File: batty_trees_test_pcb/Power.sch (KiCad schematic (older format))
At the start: 44 parts

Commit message: Finished off Power section and made up AFE schematic
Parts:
- removed J? (x3): Jumper, Connector_PinHeader_2.54mm:PinHeader_1x02_P2.54mm_Vertical, symbol Connector:Conn_01x02_Male
- added C?: 4.7uF, Capacitor_SMD:C_0805_2012Metric_Pad1.15x1.40mm_HandSolder, symbol Device:C_Small
- added C?: 0.1uF, Capacitor_SMD:C_0805_2012Metric_Pad1.15x1.40mm_HandSolder, symbol Device:C_Small
- added JP? (x4): Jumper, Connector_PinHeader_2.54mm:PinHeader_1x02_P2.54mm_Vertical, symbol Device:Jumper_NO_Small
- added R? (x3): 10k, Capacitor_SMD:C_0805_2012Metric_Pad1.15x1.40mm_HandSolder, symbol Device:R
- added TP? (x4): Test Point, OSU_SIM_BASIC:Keystone_5019, symbol Connector:TestPoint_Alt
- added U?: AD8031, Package_TO_SOT_SMD:SOT-23-5, symbol OSU_SIM_FULL:AD8031
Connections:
- net labels added: VMID
- wire segments 163 -> 185
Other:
- note added: "Alt micro USB for power"
- note added: "Buffer to supply 1/2 VDDA for VGR and AFE"
- moved on the sheet: R?, TP?

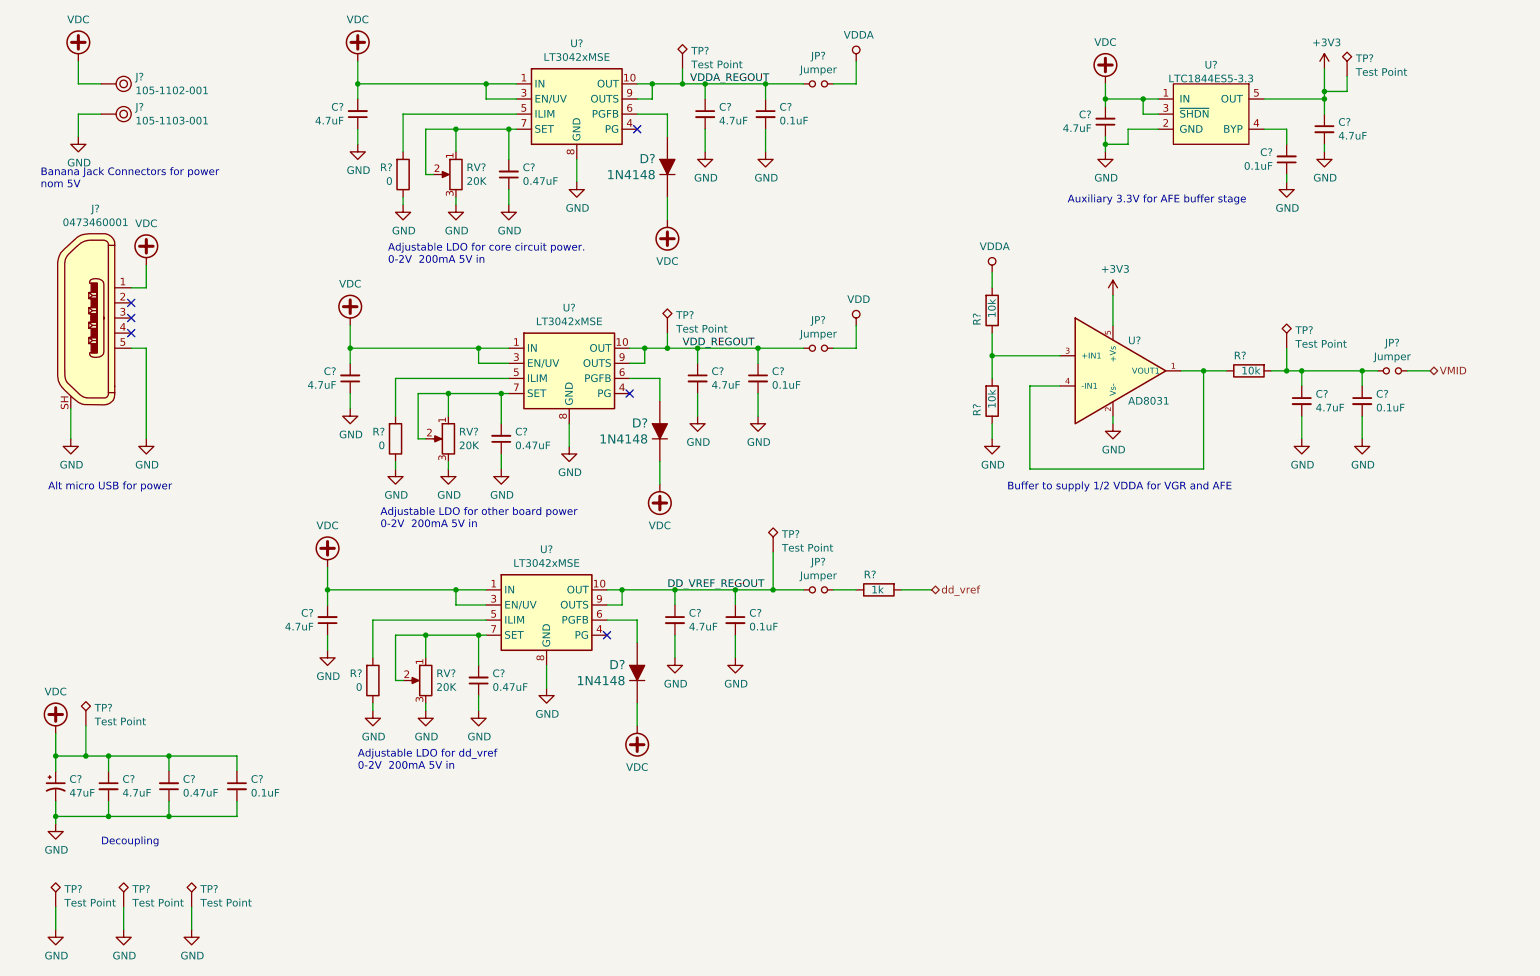
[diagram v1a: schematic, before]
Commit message: wired up chip to fpga on schematic and begininng to do layout
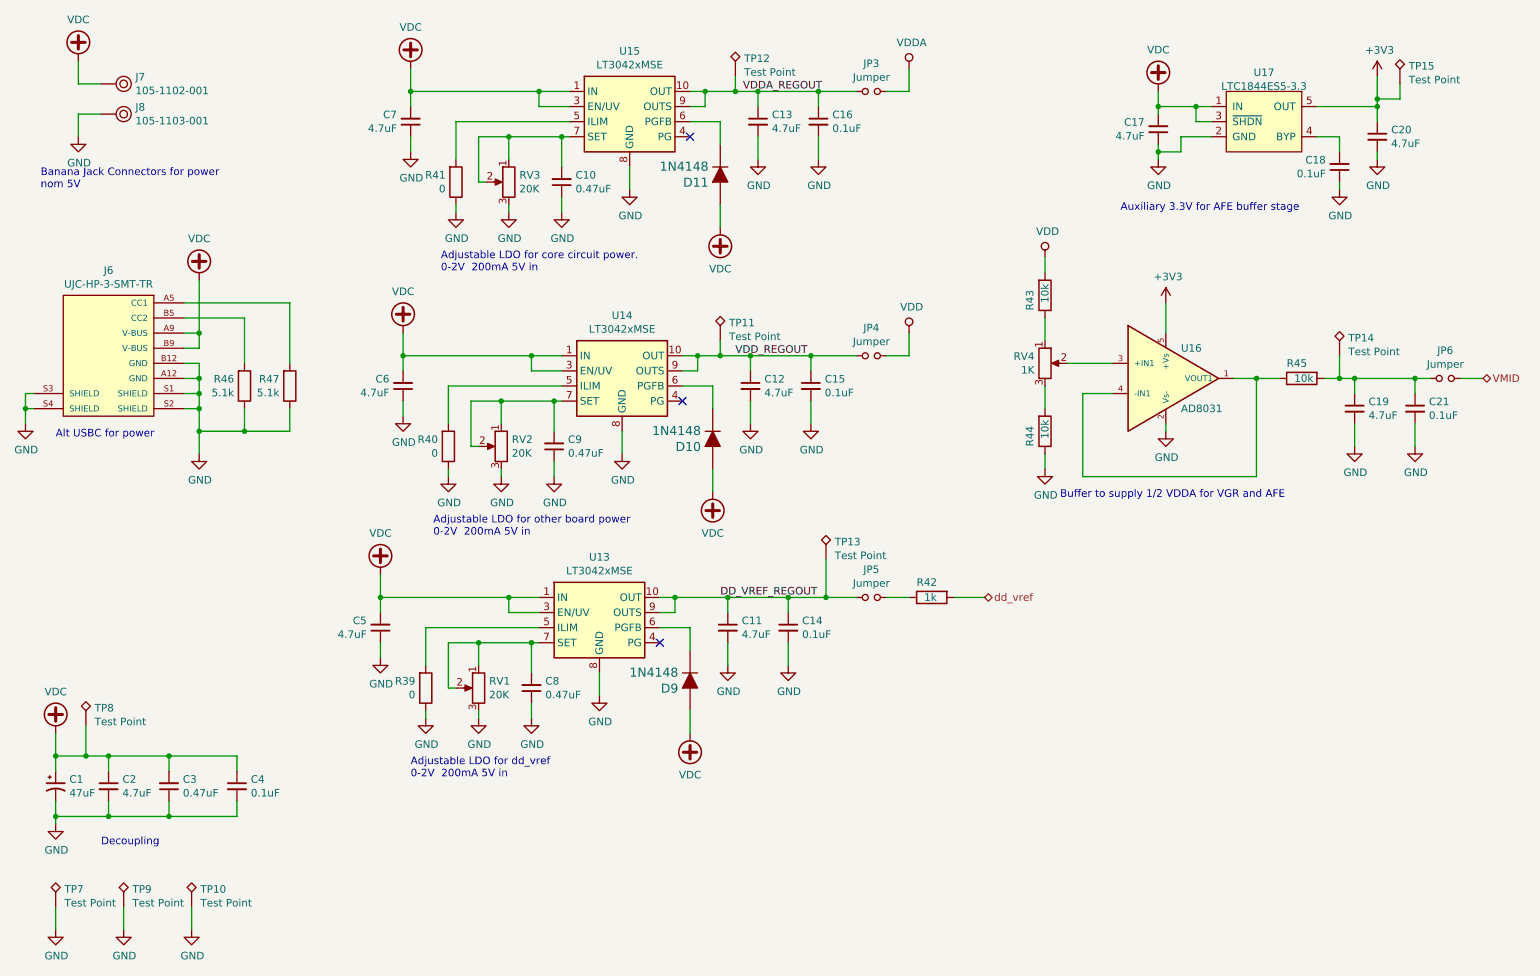
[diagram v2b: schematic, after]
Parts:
- removed J?: 0473460001, digikey-footprints:USB_Micro_B_Female_0473460001, symbol dk_USB-DVI-HDMI-Connectors:0473460001
- added J6: UJC-HP-3-SMT-TR, CUI_UJC-HP-3-SMT-TR, symbol OSU_SIM_FULL:UJC-HP-3-SMT-TR
- added R46, R47: 5.1k, Capacitor_SMD:C_0805_2012Metric_Pad1.15x1.40mm_HandSolder, symbol Device:R
- added RV4: 1K, Potentiometer_THT:Potentiometer_Bourns_3266W_Vertical, symbol Device:R_POT
- gave numbers to parts that had none: 54
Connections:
- net GND: now also J6.A12 (GND), J6.B12 (GND), J6.S1 (SHIELD), J6.S2 (SHIELD), J6.S3 (SHIELD), J6.S4 (SHIELD), R46.1, R47.1
- net VDC: now also D10.A, D11.A, D9.A, J6.A9 (V-BUS), J6.B9 (V-BUS); no longer D10.K, D11.K, D9.K
- net VDD: now also R43.2
- net VDDA: no longer R43.2
- net at U13.6 (PGFB): now also D9.K; no longer D9.A
- net at U15.6 (PGFB): now also D11.K; no longer D11.A
- net at U14.6 (PGFB): now also D10.K; no longer D10.A
- new net: J6.A5 (CC1), R47.2
- new net: J6.B5 (CC2), R46.2
- new net: RV4.2, U16.3 (+IN1)
- new net: R43.1, RV4.1
- new net: R44.2, RV4.3
- no-connect marks 6 -> 3
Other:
- note added: "Alt USBC for power"
- note removed: "Alt micro USB for power"
- moved on the sheet: C10, C11, C12, C13, C14, C15, C16, C17, C18, C19, C20, C21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

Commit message: more layout work ~90% finished
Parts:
- added C22: 0.1uF, Capacitor_SMD:C_0805_2012Metric_Pad1.15x1.40mm_HandSolder, symbol Device:C_Small
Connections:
- net +3V3: now also C22.1
- net DD_VREF_REGOUT: now also R42.1; no longer JP5.1
- net GND: now also C22.2
- net dd_vref: now also JP5.2; no longer R42.2
- new net: JP5.1, R42.2
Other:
- moved on the sheet: JP5, R42
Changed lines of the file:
@@
 	5600 4550 5850 4550
 Connection ~ 5600 4550
-Wire Wire Line
-	6250 4550 6400 4550
 $Comp
 L Device:R R42
 U 1 1 5F3F702F
-P 6550 4550
-F 0 "R42" V 6450 4650 50  0000 R CNN
-F 1 "1k" V 6550 4600 50  0000 R CNN
-F 2 "Capacitor_SMD:C_0805_2012Metric_Pad1.15x1.40mm_HandSolder" V 6480 4550 50  0001 C CNN
-F 3 "~" H 6550 4550 50  0001 C CNN
-	1    6550 4550
+P 6100 4550
+F 0 "R42" V 6000 4650 50  0000 R CNN
+F 1 "1k" V 6100 4600 50  0000 R CNN
+F 2 "Capacitor_SMD:C_0805_2012Metric_Pad1.15x1.40mm_HandSolder" V 6030 4550 50  0001 C CNN
+F 3 "~" H 6100 4550 50  0001 C CNN
+	1    6100 4550
 	0    -1   1    0
 $EndComp
@@
 L Device:Jumper_NO_Small JP5
 U 1 1 5F454C9C
-P 6150 4550
-F 0 "JP5" H 6150 4735 50  0000 C CNN
-F 1 "Jumper" H 6150 4644 50  0000 C CNN
-F 2 "Connector_PinHeader_2.54mm:PinHeader_1x02_P2.54mm_Vertical" H 6150 4550 50  0001 C CNN
-F 3 "~" H 6150 4550 50  0001 C CNN
-	1    6150 4550
+P 6500 4550
+F 0 "JP5" H 6500 4735 50  0000 C CNN
+F 1 "Jumper" H 6500 4644 50  0000 C CNN
+F 2 "Connector_PinHeader_2.54mm:PinHeader_1x02_P2.54mm_Vertical" H 6500 4550 50  0001 C CNN
+F 3 "~" H 6500 4550 50  0001 C CNN
+	1    6500 4550
 	1    0    0    -1
 $EndComp
@@
 Wire Wire Line
 	5250 1200 5400 1200
-Connection ~ 5850 4550
-Wire Wire Line
-	5850 4550 6050 4550
-Wire Wire Line
-	6700 4550 6900 4550
+Wire Wire Line
+	6600 4550 6900 4550
 $Comp
 L Connector:TestPoint_Alt TP14
@@
 Wire Wire Line
 	7450 3000 7750 3000
+Wire Wire Line
+	5850 4550 5950 4550
+Connection ~ 5850 4550
+Wire Wire Line
+	6250 4550 6400 4550
+$Comp
+L Device:C_Small C22
+U 1 1 5F53F49B
+P 8550 2600
+F 0 "C22" H 8458 2646 50  0000 R CNN
+F 1 "0.1uF" H 8458 2555 50  0000 R CNN
+F 2 "Capacitor_SMD:C_0805_2012Metric_Pad1.15x1.40mm_HandSolder" H 8550 2600 50  0001 C CNN
+F 3 "~" H 8550 2600 50  0001 C CNN
+F 4 "399-8000-1-ND" H 8550 2600 50  0001 C CNN "Digi-Key_PN"
+	1    8550 2600
+	-1   0    0    -1
+$EndComp
+$Comp
+L power:+3V3 #PWR0144
+U 1 1 5F541480
+P 8550 2450
+F 0 "#PWR0144" H 8550 2300 50  0001 C CNN
+F 1 "+3V3" H 8565 2623 50  0000 C CNN
+F 2 "" H 8550 2450 50  0001 C CNN
+F 3 "" H 8550 2450 50  0001 C CNN
+	1    8550 2450
+	1    0    0    -1
+$EndComp
+$Comp
+L power:GND #PWR0145
+U 1 1 5F54D21D
+P 8550 2800
+F 0 "#PWR0145" H 8550 2550 50  0001 C CNN
+F 1 "GND" H 8555 2627 50  0000 C CNN
+F 2 "" H 8550 2800 50  0001 C CNN
+F 3 "" H 8550 2800 50  0001 C CNN
+	1    8550 2800
+	1    0    0    -1
+$EndComp
+Wire Wire Line
+	8550 2500 8550 2450
+Wire Wire Line
+	8550 2800 8550 2700
 $EndSCHEMATC

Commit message: Layout finished and gerbers generated checking for DFM
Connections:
- net GND: no longer J6.S1 (SHIELD), J6.S2 (SHIELD), J6.S3 (SHIELD), J6.S4 (SHIELD)
- no-connect marks 3 -> 7
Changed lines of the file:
@@
 Banana Jack Connectors for power\nnom 5V\n
-$Comp
-L power:GND #PWR075
-U 1 1 5F54C291
-P 550 3400
-F 0 "#PWR075" H 550 3150 50  0001 C CNN
-F 1 "GND" H 555 3227 50  0000 C CNN
-F 2 "" H 550 3400 50  0001 C CNN
-F 3 "" H 550 3400 50  0001 C CNN
-	1    550  3400
-	1    0    0    -1
-$EndComp
-Wire Wire Line
-	550  3200 550  3300
 $Comp
 L power:GND #PWR080
@@
 	1600 3100 1700 3100
 Connection ~ 1700 3100
-Wire Wire Line
-	1700 3100 1700 3200
-Wire Wire Line
-	1600 3200 1700 3200
-Connection ~ 1700 3200
-Wire Wire Line
-	1700 3200 1700 3300
-Connection ~ 1700 3300
-Wire Wire Line
-	1700 3300 1700 3450
-Wire Wire Line
-	1600 3300 1700 3300
-Wire Wire Line
-	600  3200 550  3200
-Wire Wire Line
-	600  3300 550  3300
-Connection ~ 550  3300
-Wire Wire Line
-	550  3300 550  3400
 $Comp
 L Device:R R46
@@
 Wire Wire Line
 	8550 2800 8550 2700
+NoConn ~ 600  3300
+NoConn ~ 600  3200
+Wire Wire Line
+	1700 3100 1700 3450
+NoConn ~ 1600 3200
+NoConn ~ 1600 3300
 $EndSCHEMATC

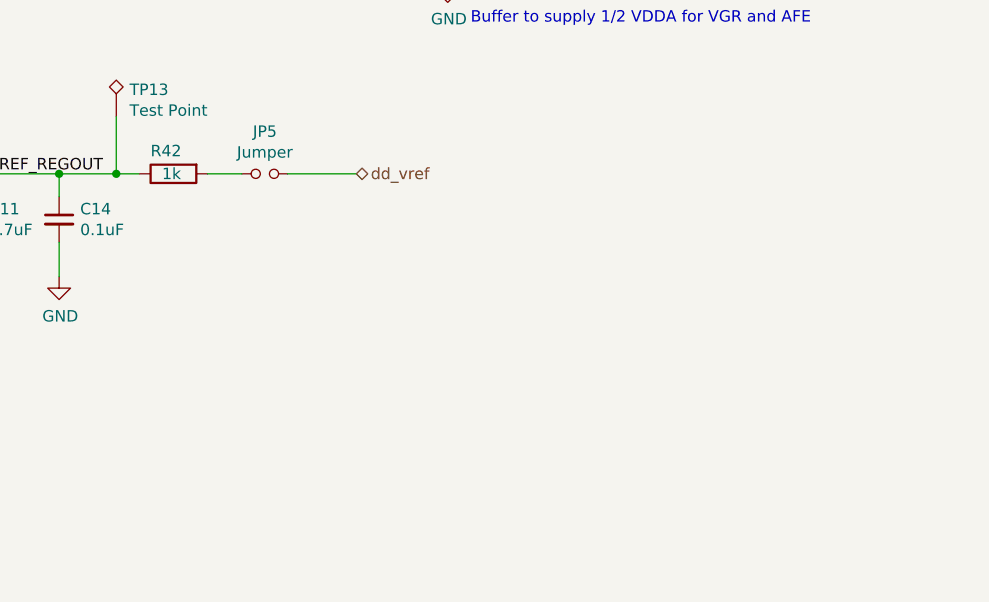
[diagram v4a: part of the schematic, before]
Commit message: all componenets updated with digikey pn bom generated
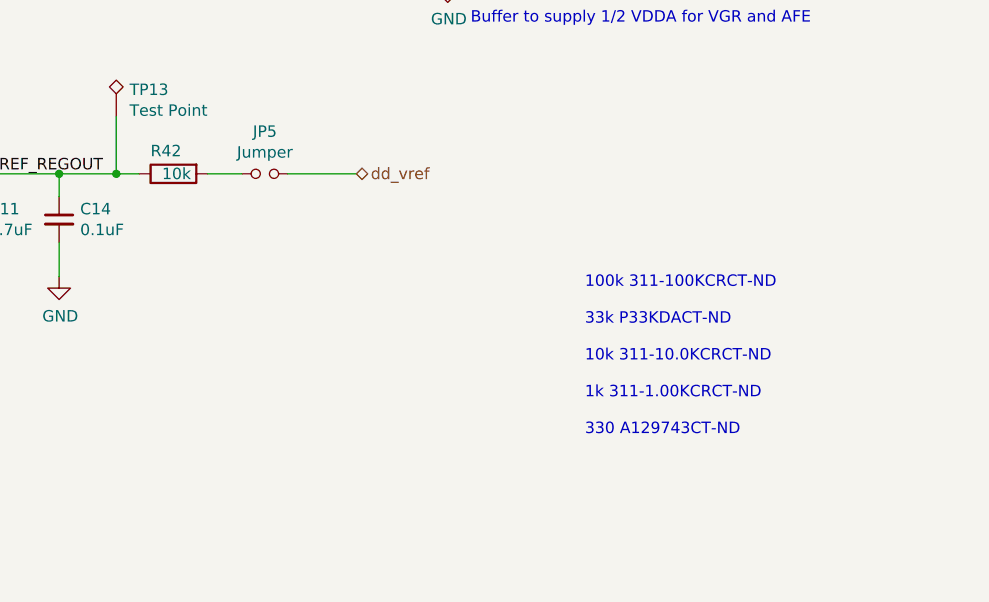
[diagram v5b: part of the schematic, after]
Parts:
- R42: value 1k -> 10k; Digi-Key_PN (none) -> 311-10.0KCRCT-ND
- R43, R44, R45: Digi-Key_PN (none) -> 311-10.0KCRCT-ND
- R46, R47: Digi-Key_PN (none) -> A126379CT-ND
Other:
- note added: "100k 311-100KCRCT-ND\n\n33k P33KDACT-ND\n\n10k 311-10.0KCRCT-ND\n\n1k 311-1.00KCRCT-ND\n\n330 A129743CT-ND"
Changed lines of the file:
@@
 P 6100 4550
 F 0 "R42" V 6000 4650 50  0000 R CNN
-F 1 "1k" V 6100 4600 50  0000 R CNN
+F 1 "10k" V 6100 4600 50  0000 R CNN
 F 2 "Capacitor_SMD:C_0805_2012Metric_Pad1.15x1.40mm_HandSolder" V 6030 4550 50  0001 C CNN
 F 3 "~" H 6100 4550 50  0001 C CNN
+F 4 "311-10.0KCRCT-ND" V 6100 4550 50  0001 C CNN "Digi-Key_PN"
 	1    6100 4550
 	0    -1   1    0
@@
 F 2 "Capacitor_SMD:C_0805_2012Metric_Pad1.15x1.40mm_HandSolder" V 7230 2550 50  0001 C CNN
 F 3 "~" H 7300 2550 50  0001 C CNN
+F 4 "311-10.0KCRCT-ND" V 7300 2550 50  0001 C CNN "Digi-Key_PN"
 	1    7300 2550
 	1    0    0    1
@@
 F 2 "Capacitor_SMD:C_0805_2012Metric_Pad1.15x1.40mm_HandSolder" V 7230 3450 50  0001 C CNN
 F 3 "~" H 7300 3450 50  0001 C CNN
+F 4 "311-10.0KCRCT-ND" V 7300 3450 50  0001 C CNN "Digi-Key_PN"
 	1    7300 3450
 	1    0    0    1
@@
 F 2 "Capacitor_SMD:C_0805_2012Metric_Pad1.15x1.40mm_HandSolder" V 8930 3100 50  0001 C CNN
 F 3 "~" H 9000 3100 50  0001 C CNN
+F 4 "311-10.0KCRCT-ND" V 9000 3100 50  0001 C CNN "Digi-Key_PN"
 	1    9000 3100
 	0    -1   1    0
@@
 F 2 "Capacitor_SMD:C_0805_2012Metric_Pad1.15x1.40mm_HandSolder" V 1930 3150 50  0001 C CNN
 F 3 "~" H 2000 3150 50  0001 C CNN
+F 4 "A126379CT-ND" H 2000 3150 50  0001 C CNN "Digi-Key_PN"
 	1    2000 3150
 	1    0    0    1
@@
 F 2 "Capacitor_SMD:C_0805_2012Metric_Pad1.15x1.40mm_HandSolder" V 2230 3150 50  0001 C CNN
 F 3 "~" H 2300 3150 50  0001 C CNN
+F 4 "A126379CT-ND" H 2300 3150 50  0001 C CNN "Digi-Key_PN"
 	1    2300 3150
 	1    0    0    1
@@
 NoConn ~ 1600 3200
 NoConn ~ 1600 3300
+Text Notes 7900 5700 0    50   ~ 0
+100k 311-100KCRCT-ND\n\n33k P33KDACT-ND\n\n10k 311-10.0KCRCT-ND\n\n1k 311-1.00KCRCT-ND\n\n330 A129743CT-ND
 $EndSCHEMATC
